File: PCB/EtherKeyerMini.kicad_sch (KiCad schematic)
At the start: 34 parts, among them J1 Key Output, J2 Paddle Input, J3 UART, Q1 VP2106N3, Q2 2N7000, Q3 2N7000, U1 ATtiny85

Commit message: Schematic update
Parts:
- R10: value 100k -> 1M
- R5: value 100k -> 47k
- R7: value 10k -> 3.3k
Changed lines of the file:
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@@
   (title_block
     (title "EtherKeyer Mini")
-    (date "2024-01-09")
+    (date "2024-01-13")
     (rev "A")
     (company "Etherkit LLC")
@@
       (effects (font (size 1.27 1.27)))
     )
-    (property "Value" "100k" (at 87.63 57.15 90)
+    (property "Value" "47k" (at 87.63 57.15 90)
       (effects (font (size 1.27 1.27)))
     )
@@
       (effects (font (size 1.27 1.27)) (justify right))
     )
-    (property "Value" "100k" (at 173.736 69.85 0)
+    (property "Value" "1M" (at 173.736 69.85 0)
       (effects (font (size 1.27 1.27)) (justify right))
     )
@@
   (symbol (lib_id "Device:R_US") (at 102.87 102.87 0) (mirror y) (unit 1)
     (in_bom yes) (on_board yes) (dnp no) (fields_autoplaced)
-    (property "Reference" "R7" (at 100.33 101.6 0)
-      (effects (font (size 1.27 1.27)) (justify left))
-    )
-    (property "Value" "10k" (at 100.33 104.14 0)
-      (effects (font (size 1.27 1.27)) (justify left))
+    (property "Reference" "R7" (at 105.41 101.6 0)
+      (effects (font (size 1.27 1.27)) (justify right))
+    )
+    (property "Value" "3.3k" (at 105.41 104.14 0)
+      (effects (font (size 1.27 1.27)) (justify right))
     )
     (property "Footprint" "Resistor_THT:R_Axial_DIN0207_L6.3mm_D2.5mm_P2.54mm_Vertical" (at 101.854 103.124 90)

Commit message: Rev B PCB
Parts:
- removed D1: 1N5711, Diode_THT:D_DO-35_SOD27_P7.62mm_Horizontal, symbol Device:D_Schottky
- removed Q1: VP2106N3, Package_TO_SOT_THT:TO-92_Inline, symbol Device:Q_PMOS_SGD
- removed R1: 10k, Resistor_THT:R_Axial_DIN0207_L6.3mm_D2.5mm_P2.54mm_Vertical, symbol Device:R_US
- added SW1: Power Switch, EtherkitKicadLibrary:E-Switch_LC1258, symbol Switch:SW_SPDT_321
- C1: value 100n -> 10u; footprint Capacitor_THT:C_Rect_L7.0mm_W2.5mm_P5.00mm -> Capacitor_THT:CP_Radial_D5.0mm_P2.50mm; symbol Device:C_Small -> Device:C_Polarized_Small_US
- C4, C5: value 10n -> 100n
- J3: footprint Connector_PinHeader_2.54mm:PinHeader_1x05_P2.54mm_Horizontal -> Connector_PinHeader_2.54mm:PinHeader_1x04_P2.54mm_Horizontal; symbol Connector_Generic:Conn_01x05 -> Connector_Generic:Conn_01x04
- Q2, Q3: value 2N7000 -> 2N4401; symbol Transistor_FET:2N7000 -> Device:Q_NPN_EBC
- R6, R9: value 100k -> 10k
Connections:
- net +5V is gone; now on net GND: J3.4 (Pin_4)
- net GND: no longer J3.5 (Pin_5), R6.2, R9.2
- net VDD: now also SW1.1 (C)
- net at Q3.2 (B), R9.1: no longer U1.3 (PB4)
- net at BT1.1 (+): now also SW1.2 (B)
- net at Q2.2 (B), R6.1: no longer U1.2 (PB3)
- new net: R9.2, U1.3 (PB4)
- new net: R6.2, U1.2 (PB3)
- no-connect marks 0 -> 1
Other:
- note added: "Resistors R3, R4, R5, and R8 at least 1% tolerance"
- note removed: "All resistors at least 1% tolerance"
- moved on the sheet: R2, R6, R7, R9, SP1

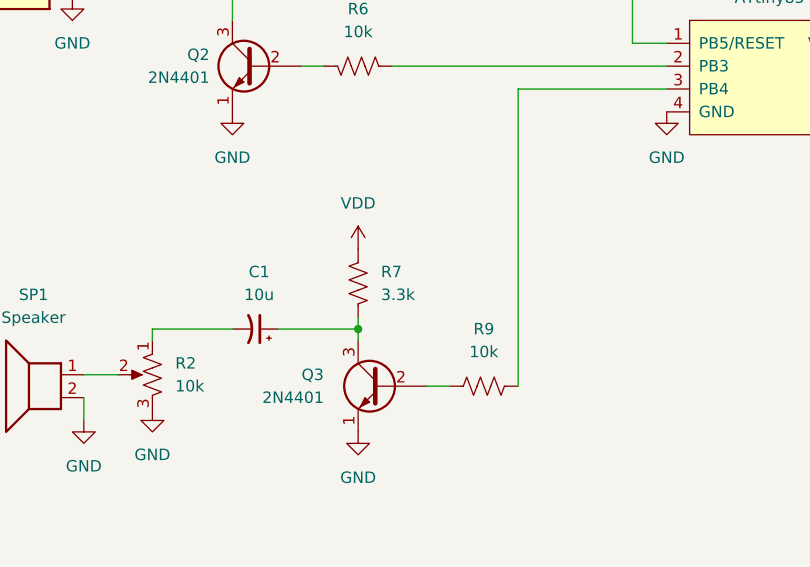
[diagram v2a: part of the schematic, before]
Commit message: Update schematic, include built firmware
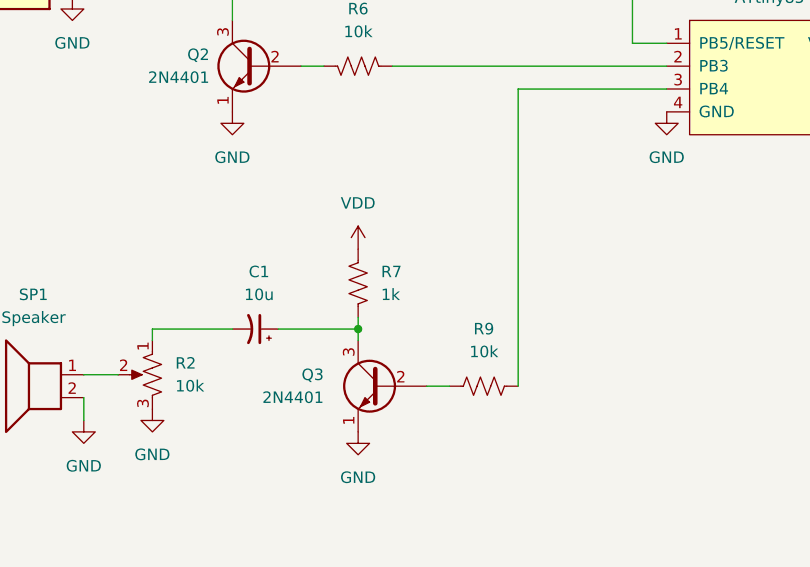
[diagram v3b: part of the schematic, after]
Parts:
- R7: value 3.3k -> 1k
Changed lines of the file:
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@@
 		(fields_autoplaced yes)
 		(property "Reference" "R7"
-			(at 95.25 101.6 0)
+			(at 95.25 101.5999 0)
 			(effects
 				(font
@@
 			)
 		)
-		(property "Value" "3.3k"
-			(at 95.25 104.14 0)
+		(property "Value" "1k"
+			(at 95.25 104.1399 0)
 			(effects
 				(font

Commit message: Documentation update for Beta
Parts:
- C1: value 10u -> 1u
- U1: value ATtiny85 -> ATtiny85V
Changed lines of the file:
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@@
 	(title_block
 		(title "EtherKeyer Mini")
-		(date "2024-05-28")
+		(date "2024-09-03")
 		(rev "B")
 		(company "Etherkit LLC")
@@
 			)
 		)
-		(property "Value" "10u"
+		(property "Value" "1u"
 			(at 81.7118 104.14 90)
 			(effects
@@
 			)
 		)
-		(property "Value" "ATtiny85"
+		(property "Value" "ATtiny85V"
 			(at 138.43 71.12 0)
 			(effects

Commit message: Rev C PCB
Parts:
- removed C4, C5: 100n, Capacitor_THT:C_Rect_L7.0mm_W2.5mm_P5.00mm, symbol Device:C_Small
- removed Q3: 2N4401, Package_TO_SOT_THT:TO-92_Inline, symbol Device:Q_NPN_EBC
- removed R2: 10k, EtherkitKicadLibrary:Piher_N6L50T0C-103, symbol Device:R_Potentiometer_US
- removed R4: 22k, Resistor_THT:R_Axial_DIN0207_L6.3mm_D2.5mm_P2.54mm_Vertical, symbol Device:R_US
- removed R5: 47k, Resistor_THT:R_Axial_DIN0207_L6.3mm_D2.5mm_P2.54mm_Vertical, symbol Device:R_US
- removed R7: 1k, Resistor_THT:R_Axial_DIN0207_L6.3mm_D2.5mm_P2.54mm_Vertical, symbol Device:R_US
- removed R9: 10k, Resistor_THT:R_Axial_DIN0207_L6.3mm_D2.5mm_P2.54mm_Vertical, symbol Device:R_US
- removed SW1: Power Switch, EtherkitKicadLibrary:E-Switch_LC1258, symbol Switch:SW_SPDT_321
- removed U1: ATtiny85V, Package_DIP:DIP-8_W7.62mm_LongPads, symbol EtherkitKicadLibrary:ATtiny85
- added C2: 100n, Capacitor_THT:C_Rect_L7.0mm_W2.5mm_P5.00mm, symbol Device:C_Small
- added D1, D2: 1N5711, Diode_THT:D_DO-35_SOD27_P7.62mm_Horizontal, symbol Device:D_Schottky
- added JP1: SolderJumper_2_Bridged, Jumper:SolderJumper-2_P1.3mm_Bridged_RoundedPad1.0x1.5mm, symbol Jumper:SolderJumper_2_Bridged
- added JP2, JP3: SolderJumper_2_Bridged, Jumper:SolderJumper-2_P1.3mm_Open_RoundedPad1.0x1.5mm, symbol Jumper:SolderJumper_2_Open
- added Q1: 2N4401, Package_TO_SOT_THT:TO-92_Inline, symbol Device:Q_NPN_EBC
- added R1: 10k, Resistor_THT:R_Axial_DIN0207_L6.3mm_D2.5mm_P2.54mm_Vertical, symbol Device:R_US
- added U1: ATtiny3226-S, Package_SO:SOIC-20W_7.5x12.8mm_P1.27mm, symbol MCU_Microchip_ATtiny:ATtiny3226-S
- C1: value 1u -> 4.7u; footprint Capacitor_THT:CP_Radial_D5.0mm_P2.50mm -> Capacitor_THT:CP_Radial_D6.3mm_P2.50mm
- J2: value Paddle Input -> Paddle Input/UART; footprint EtherkitKicadLibrary:Kycon_STX-3120-3B -> EtherkitKicadLibrary:SameSky_SJ-43514; symbol Connector_Audio:AudioJack3 -> Connector_Audio:AudioJack3_Ground
- J3: value UART -> UPDI; footprint Connector_PinHeader_2.54mm:PinHeader_1x04_P2.54mm_Horizontal -> Connector_PinSocket_2.54mm:PinSocket_1x04_P2.54mm_Vertical
- R3: value 10k -> 470
- SP1: value Speaker -> Piezo Speaker
- renumbered C2 to C3, C3 to C4, R6 to R2, R8 to R4, R10 to R5
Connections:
- net DTR: now also J2.S; no longer J3.1 (Pin_1)
- net GND: now also C1.2, J2.G, S1.1, S2.1, S3.1, C2.1, Q1.1 (E), U1.20 (GND); no longer J2.S, R3.1, SP1.2
- net RX: now also JP3.1 (A), U1.9 (PB2); no longer J3.2 (Pin_2)
- net TX: now also JP2.1 (A), U1.8 (PB3); no longer J3.3 (Pin_3)
- net VDD: now also BT1.1 (+), C1.1, SP1.1, C2.2, D2.1 (K), U1.1 (VCC); no longer C4.1
- net at R3.2: now also J3.3 (Pin_3), D1.2 (A), JP3.2 (B); no longer S1.1
- net KEY: now reaches R2.2
- net KEY: now also U1.4 (PA6)
- net at R5.2: now also C4.1, U1.6 (PB5)
- net at J1.T, Q2.3 (C): now also JP1.2 (B); no longer J1.R
- new net: Q1.3 (C), SP1.2
- new net: J1.R, JP1.1 (A)
- new net: R3.1, U1.16 (~{RESET}/PA0)
- new net: C3.1, R4.2, U1.7 (PB4)
- new net: Q1.2 (B), R1.1
- new net: D1.1 (K), J3.2 (Pin_2), JP2.2 (B)
- new net: D2.2 (A), J3.1 (Pin_1)
- new net: S3.2, U1.14 (PC2)
- new net: S1.2, U1.12 (PC0)
- new net: S2.2, U1.13 (PC1)
- new net SIDETONE: R1.2, U1.5 (PA7)
- no-connect marks 1 -> 8
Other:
- note added: "GND"
- note added: "RX"
- note added: "TX"
- note added: "VCC"
- note removed: "Resistors R3, R4, R5, and R8 at least 1% tolerance"
- moved on the sheet: BT1, C3, C4, J1, Q2, R2, R4, R5, S1, S2, S3, SP1
